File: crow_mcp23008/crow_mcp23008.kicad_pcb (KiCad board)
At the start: 2 copper layers, 30 x 103.5 mm, 26 parts, among them J1 Conn_02x03_Odd_Even, J2 MJ-3523-SMT-TR, J3 MJ-3523-SMT-TR, J4 MJ-3523-SMT-TR, J5 MJ-3523-SMT-TR, J6 MJ-3523-SMT-TR, J7 MJ-3523-SMT-TR, J8 MJ-3523-SMT-TR, J9 Conn_02x05_Odd_Even, U1 MCP23008-xP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

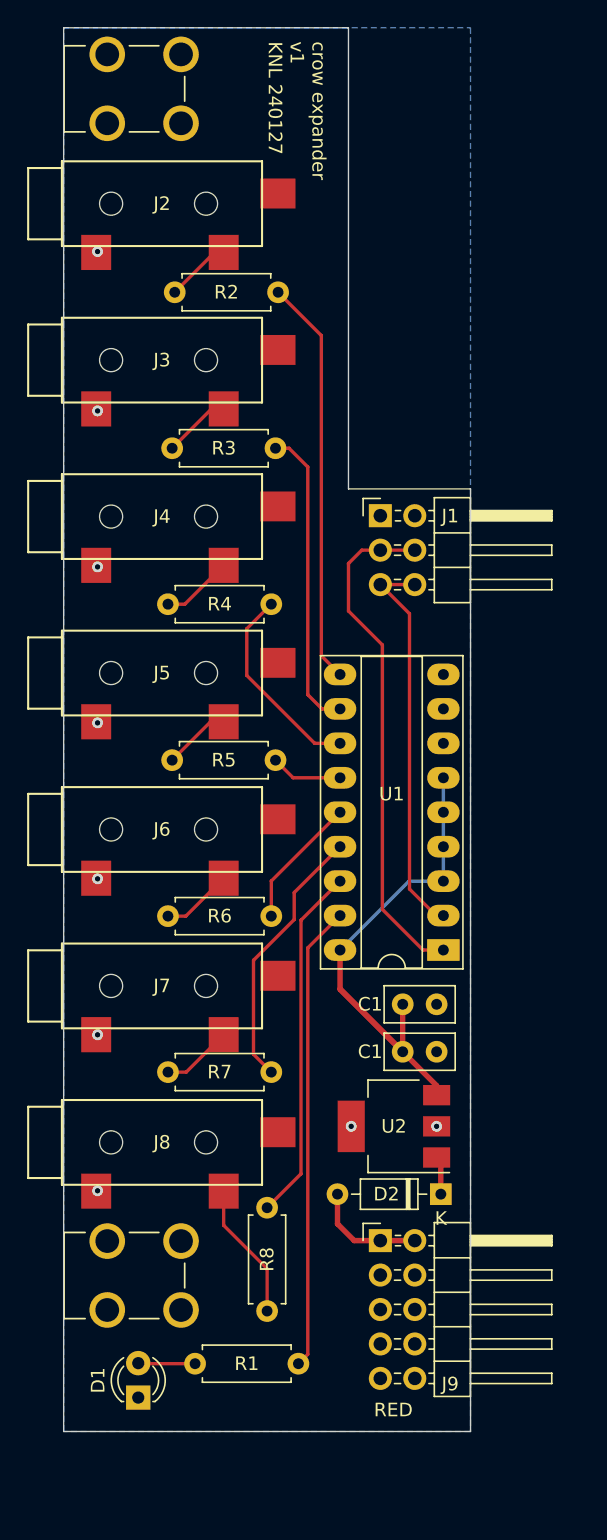
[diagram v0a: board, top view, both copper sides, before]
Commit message: v1.1
all SMT w/ LED's
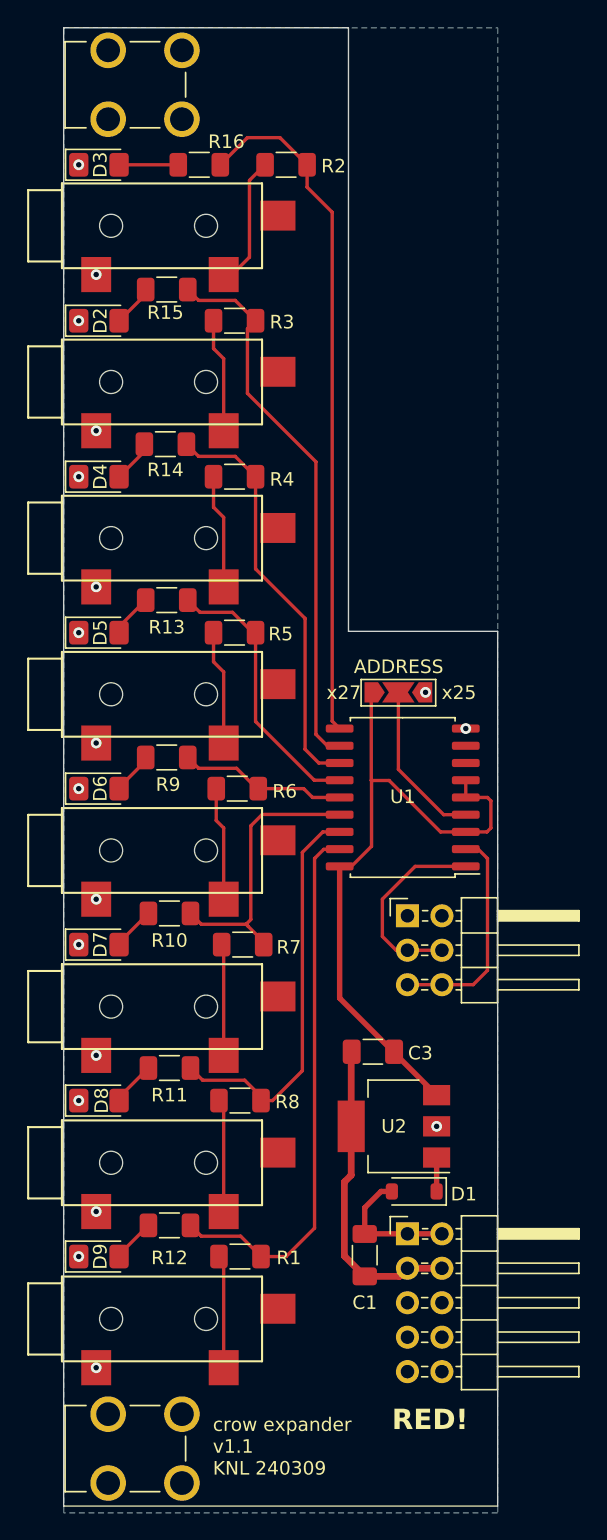
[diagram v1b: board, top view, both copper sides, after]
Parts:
- removed the C1 at (118.0, 112.0)
- removed the C1 at (118.0, 115.5)
- removed G***: LOGO, knl:beef
- added C1: C, Capacitor_SMD:C_1206_3216Metric_Pad1.33x1.80mm_HandSolder, F.Cu at (115.2, 130.5)
- added C3: C, Capacitor_SMD:C_1206_3216Metric_Pad1.33x1.80mm_HandSolder, F.Cu at (115.8, 115.5)
- added D3: LED, LED_SMD:LED_1206_3216Metric_Pad1.42x1.75mm_HandSolder, F.Cu at (95.6, 50.1)
- added D4: LED, LED_SMD:LED_1206_3216Metric_Pad1.42x1.75mm_HandSolder, F.Cu at (95.6, 73.1)
- added D5: LED, LED_SMD:LED_1206_3216Metric_Pad1.42x1.75mm_HandSolder, F.Cu at (95.6, 84.6)
- added D6: LED, LED_SMD:LED_1206_3216Metric_Pad1.42x1.75mm_HandSolder, F.Cu at (95.6, 96.1)
- added D7: LED, LED_SMD:LED_1206_3216Metric_Pad1.42x1.75mm_HandSolder, F.Cu at (95.6, 107.6)
- added D8: LED, LED_SMD:LED_1206_3216Metric_Pad1.42x1.75mm_HandSolder, F.Cu at (95.6, 119.1)
- added D9: LED, LED_SMD:LED_1206_3216Metric_Pad1.42x1.75mm_HandSolder, F.Cu at (95.6, 130.6)
- added J10: MJ-3523-SMT-TR, Connector_Audio:CONN_MJ-3523_CUD, F.Cu at (100.2, 135.2)
- added JP2: SolderJumper_3_Open, Jumper:SolderJumper-3_P2.0mm_Open_TrianglePad1.0x1.5mm_NumberLabels, F.Cu at (117.7, 89.0)
- added R10: R, Resistor_SMD:R_1206_3216Metric_Pad1.30x1.75mm_HandSolder, F.Cu at (100.8, 105.3)
- added R11: R, Resistor_SMD:R_1206_3216Metric_Pad1.30x1.75mm_HandSolder, F.Cu at (100.8, 116.7)
- added R12: R, Resistor_SMD:R_1206_3216Metric_Pad1.30x1.75mm_HandSolder, F.Cu at (100.8, 128.3)
- added R13: R, Resistor_SMD:R_1206_3216Metric_Pad1.30x1.75mm_HandSolder, F.Cu at (100.6, 82.2)
- added R14: R, Resistor_SMD:R_1206_3216Metric_Pad1.30x1.75mm_HandSolder, F.Cu at (100.5, 70.7)
- added R15: R, Resistor_SMD:R_1206_3216Metric_Pad1.30x1.75mm_HandSolder, F.Cu at (100.6, 59.3)
- added R16: R, Resistor_SMD:R_1206_3216Metric_Pad1.30x1.75mm_HandSolder, F.Cu at (103.0, 50.1)
- added R9: R, Resistor_SMD:R_1206_3216Metric_Pad1.30x1.75mm_HandSolder, F.Cu at (100.6, 93.8)
- D1: value LED -> MBR0540; footprint LED_THT:LED_D3.0mm_FlatTop -> Diode_SMD:D_SOD-123
- D2: value 1N4148 -> LED; footprint Diode_THT:D_DO-35_SOD27_P7.62mm_Horizontal -> LED_SMD:LED_1206_3216Metric_Pad1.42x1.75mm_HandSolder
- R1, R2, R3, R4, R5, R6, R7, R8: footprint Resistor_THT:R_Axial_DIN0207_L6.3mm_D2.5mm_P7.62mm_Horizontal -> Resistor_SMD:R_1206_3216Metric_Pad1.30x1.75mm_HandSolder
- U1: footprint Package_DIP:DIP-18_W7.62mm_Socket_LongPads -> Package_SO:SOIC-18W_7.5x11.6mm_P1.27mm
- moved D2 69.2 mm to (95.6, 61.6), turned to 0 degrees
- moved J1 29.6 mm to (118.3, 105.5)
- moved D1 25.4 mm to (118.8, 125.8), turned to 180 degrees
- moved KEYSTONE7773 12.8 mm to (99.0, 144.8)
- moved U1 11.6 mm to (118.0, 96.8)
- moved R5 9.87 mm to (105.6, 84.6)
- moved R3 9.87 mm to (105.6, 61.6)
- moved R4 9.78 mm to (105.6, 73.1)
- moved R6 9.73 mm to (105.8, 96.1)
- moved R7 9.63 mm to (106.2, 107.6)
- moved R2 9.42 mm to (109.4, 50.1)
- moved R1 9.00 mm to (106.0, 130.6)
- moved R8 8.15 mm to (106.0, 119.1), turned to 180 degrees
- moved J9 2.06 mm to (118.3, 128.9)
- moved J2 1.63 mm to (100.2, 54.6)
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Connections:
- D1 pad 1: GND -> Net-(D1-K)
- D2 pad 1: Net-(D2-K) -> GND
- J9 pad 1: Net-(D2-A) -> Net-(D1-A)
- J9 pad 2: Net-(D2-A) -> Net-(D1-A)
- R1 pad 2: Net-(D1-A) -> Net-(J10-T)
- U1 pad 4: +5V -> Net-(JP2-C)
- U2 pad 1: Net-(D2-K) -> Net-(D1-K)
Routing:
- net GND: track 0.00 -> 23.3 mm, vias 9 -> 19
- net Net-(J1-Pin_3): track 36.8 -> 14.7 mm
- net Net-(U1-GP0): track 30.1 -> 50.6 mm
- net Net-(U1-GP1): track 22.6 -> 41.3 mm
- net Net-(U1-GP2): track 15.0 -> 31.0 mm
- net Net-(U1-GP3): track 5.30 -> 20.6 mm
- net Net-(J1-Pin_5): track 29.2 -> 16.5 mm
- net Net-(JP2-C): track 0.00 -> 12.0 mm
- net +5V: track 41.2 -> 50.7 mm
- net Net-(J10-T): track 0.00 -> 8.74 mm
- net Net-(D1-A): track 4.21 -> 10.3 mm
- net Net-(U1-GP7): track 34.3 -> 39.9 mm
- net Net-(D2-A): track 8.40 -> 3.51 mm
- net Net-(J2-T): track 5.09 -> 9.98 mm
- net Net-(D3-A): track 0.00 -> 4.36 mm
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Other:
- board size 30 x 103.5 mm -> 32 x 109 mm
- board text added: "ADDRESS"
- board text added: "RED!"
- board text added: "crow expander v1.1 KNL 240309"
- board text added: "x25"
- board text added: "x27"
- board text removed: "RED"
- board text removed: "crow expander v1 KNL 240127"
